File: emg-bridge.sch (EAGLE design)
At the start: 23 parts, among them J1 RJ25_4X1, J2 RJ25_4X1, J3 M03_0.156IN-RA, U1 ADM660ARZ

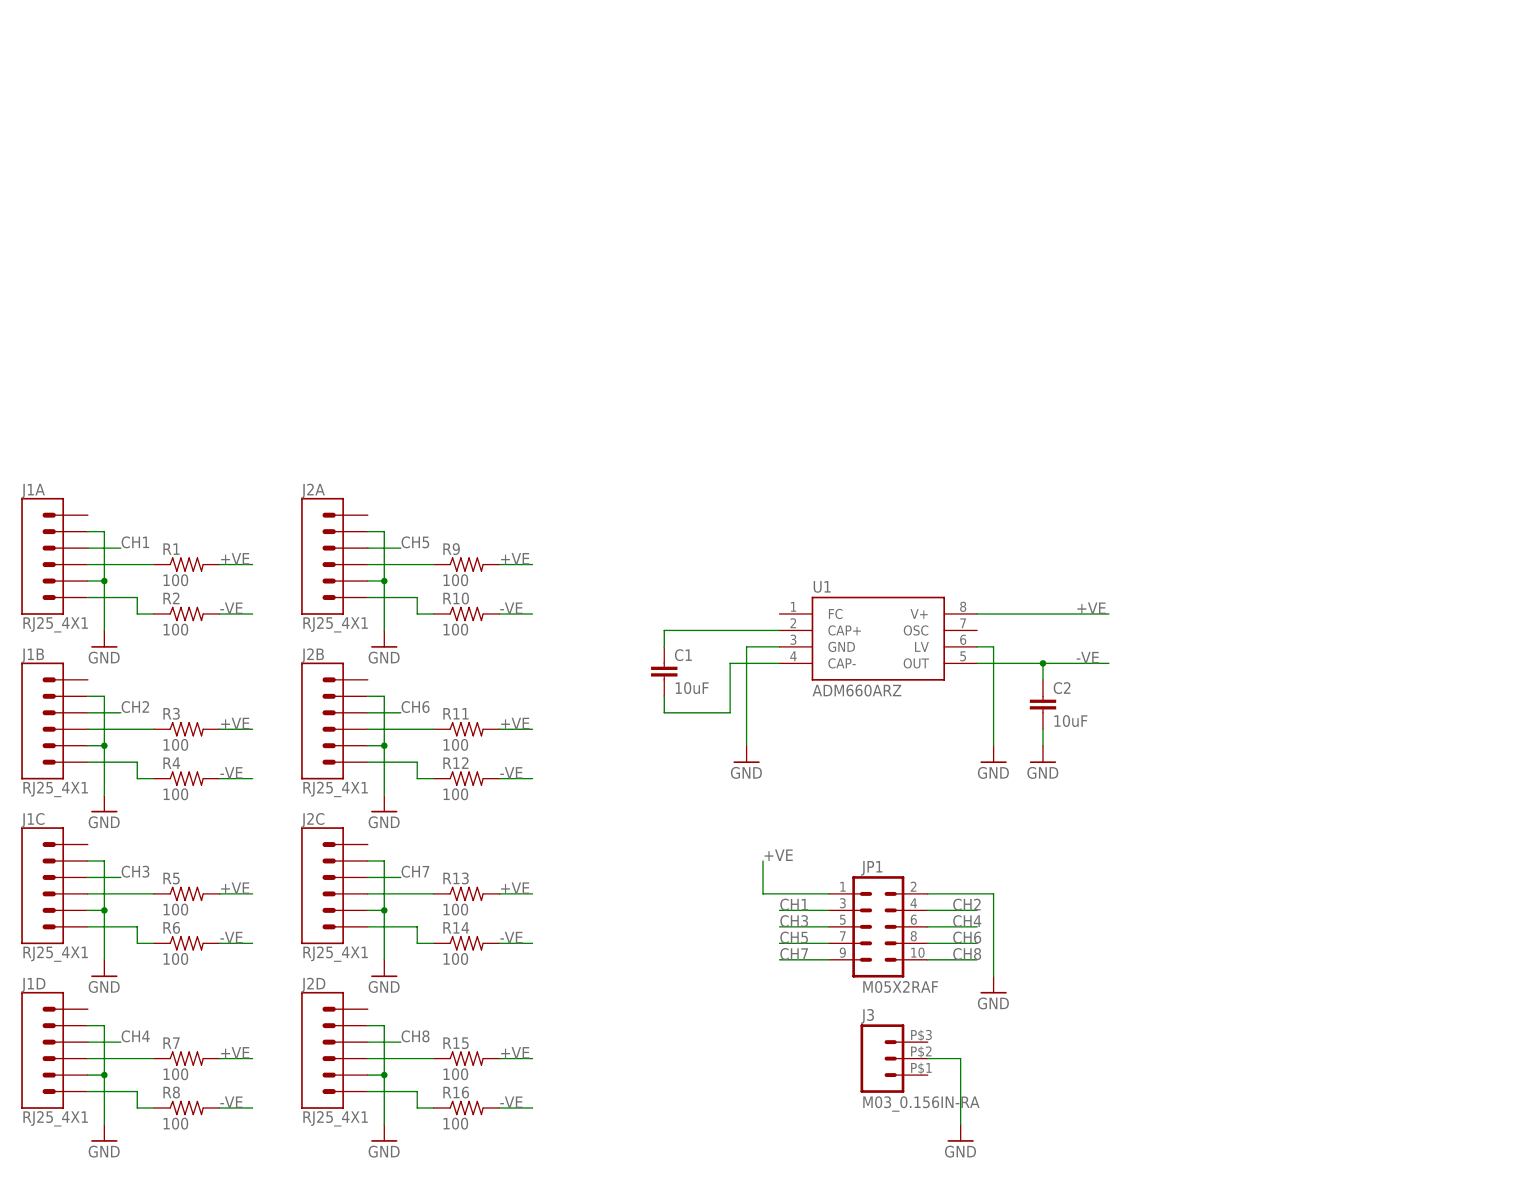
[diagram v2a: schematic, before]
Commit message: Updated for eagle-lib changes. Finished up schematic.
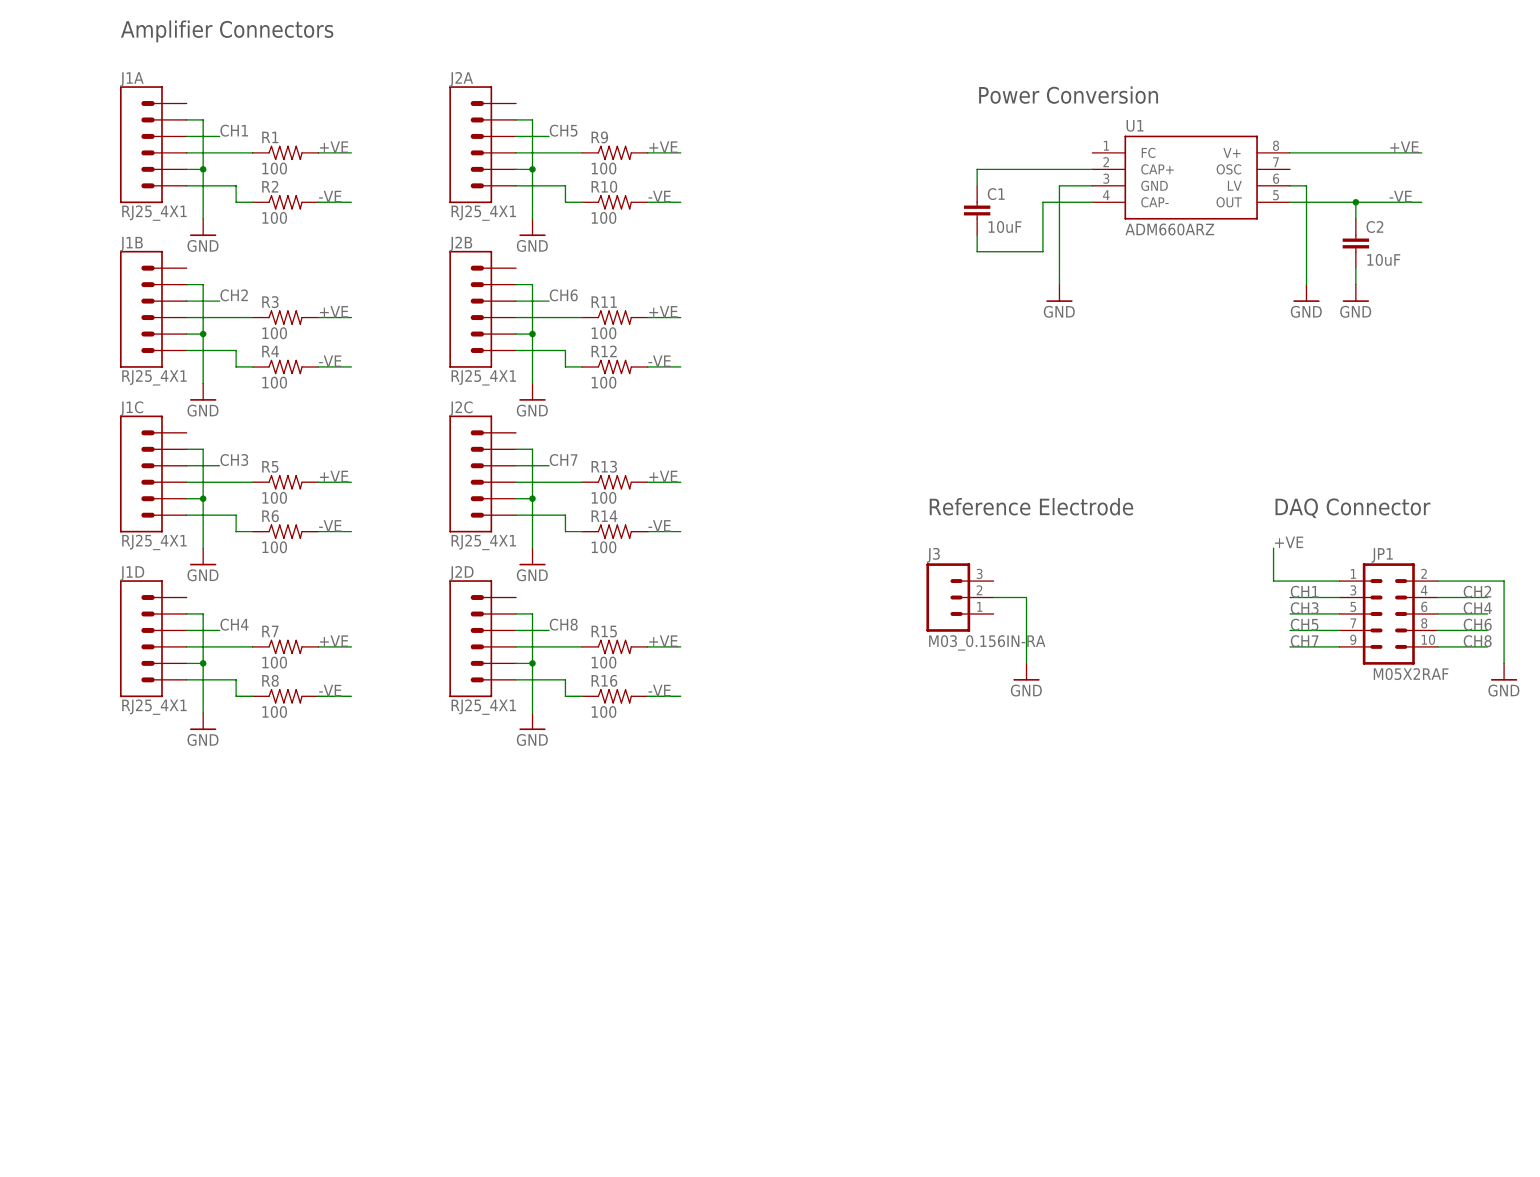
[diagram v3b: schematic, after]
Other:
- note added: "Amplifier Connectors"
- note added: "DAQ Connector"
- note added: "Power Conversion"
- note added: "Reference Electrode"
- moved on the sheet: C1, C2, J1A, J1B, J1C, J1D, J2A, J2B, J2C, J2D, J3, JP1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

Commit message: Finished up layout and routing. Revision 1 complete.
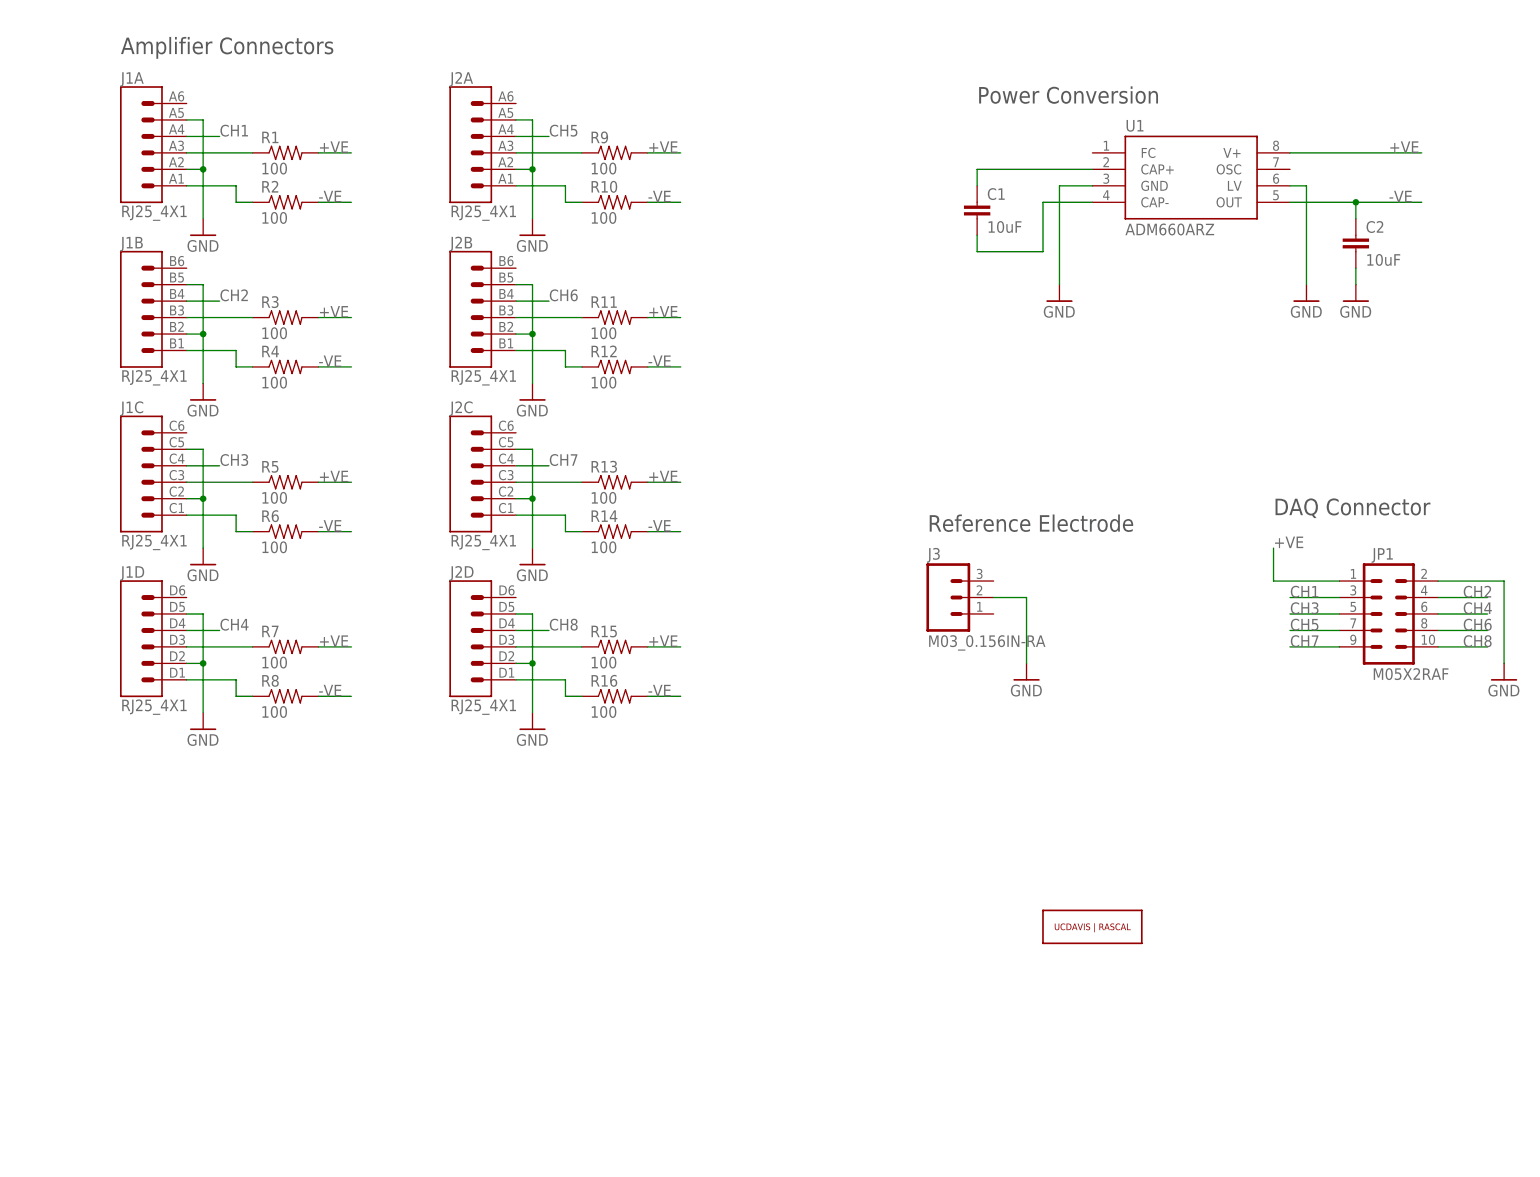
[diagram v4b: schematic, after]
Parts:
- added U$1: UCDAVIS-RASCAL_LOGO-2LINE, ucdrascal-eagle-lib:UCDAVIS-RASCAL_LOGO-2LINE
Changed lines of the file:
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@@
 <part name="J3" library="eagle-lib" deviceset="M03" device="_0.156IN-RA"/>
 <part name="JP1" library="SparkFun-Connectors" deviceset="M05X2" device="RAF"/>
-<part name="FRAME1" library="frames" deviceset="FRAME_A_L" device=""/>
+<part name="FRAME1" library="frames" deviceset="FRAME_A_L" device="" value="FRAME"/>
+<part name="U$1" library="ucdrascal-eagle-lib" deviceset="UCDAVIS-RASCAL_LOGO" device="-2LINE"/>
 </parts>
 <sheets>
 <sheet>
 <plain>
-<text x="30.48" y="177.8" size="2.54" layer="97">Amplifier Connectors</text>
+<text x="30.48" y="175.26" size="2.54" layer="97">Amplifier Connectors</text>
 <text x="162.56" y="167.64" size="2.54" layer="97">Power Conversion</text>
 <text x="208.28" y="104.14" size="2.54" layer="97">DAQ Connector</text>
-<text x="154.94" y="104.14" size="2.54" layer="97">Reference Electrode</text>
+<text x="154.94" y="101.6" size="2.54" layer="97">Reference Electrode</text>
 </plain>
 <instances>
@@
 <instance part="FRAME1" gate="G$1" x="0" y="0"/>
 <instance part="FRAME1" gate="G$2" x="172.72" y="0"/>
+<instance part="U$1" gate="G$1" x="180.34" y="40.64"/>
 </instances>
 <busses>

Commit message: Added channel numbers on silkscreen.
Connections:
- net GND: now also J3.1, J3.3
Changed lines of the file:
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@@
 <setting verticaltext="up"/>
 </settings>
-<grid distance="0.1" unitdist="inch" unit="inch" style="lines" multiple="1" display="yes" altdistance="0.01" altunitdist="inch" altunit="inch"/>
+<grid distance="0.1" unitdist="inch" unit="inch" style="lines" multiple="1" display="no" altdistance="0.01" altunitdist="inch" altunit="inch"/>
 <layers>
 <layer number="1" name="Top" color="4" fill="1" visible="no" active="no"/>
@@
 <wire x1="165.1" y1="91.44" x2="170.18" y2="91.44" width="0.1524" layer="91"/>
 <pinref part="GND12" gate="1" pin="GND"/>
-<wire x1="170.18" y1="81.28" x2="170.18" y2="91.44" width="0.1524" layer="91"/>
+<wire x1="170.18" y1="81.28" x2="170.18" y2="88.9" width="0.1524" layer="91"/>
 <pinref part="J3" gate="G$1" pin="2"/>
+<pinref part="J3" gate="G$1" pin="3"/>
+<wire x1="170.18" y1="88.9" x2="170.18" y2="91.44" width="0.1524" layer="91"/>
+<wire x1="165.1" y1="93.98" x2="170.18" y2="93.98" width="0.1524" layer="91"/>
+<wire x1="170.18" y1="93.98" x2="170.18" y2="91.44" width="0.1524" layer="91"/>
+<junction x="170.18" y="91.44"/>
+<pinref part="J3" gate="G$1" pin="1"/>
+<wire x1="165.1" y1="88.9" x2="170.18" y2="88.9" width="0.1524" layer="91"/>
+<junction x="170.18" y="88.9"/>
 </segment>
 <segment>
